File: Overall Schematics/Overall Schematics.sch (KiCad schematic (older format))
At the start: 31 parts, among them J1 WattMeter1_Output, J2 WattMeter2_Output, J3 Intel_Buck_Converter_Input, J4 WattMeter1_Input, J5 WattMeter2_Input, M1 Stepper_Motor_bipolar, M2 Stepper_Motor_bipolar, M3 LinActuator12V, M4 LinActuator12V, M5 LinActuator12V, M6 Motor_DC, M7 Motor_DC, M8 Motor_DC, M9 Motor_DC, SW1 SW_DPST, U1 Teensy4.1, U10 VNH52019, U2 36v4SMD, U3 36v4SMD, U4 VNH52019, U5 VNH52019, U6 VNH52019, U7 VNH52019, U8 VNH52019, U9 VNH52019

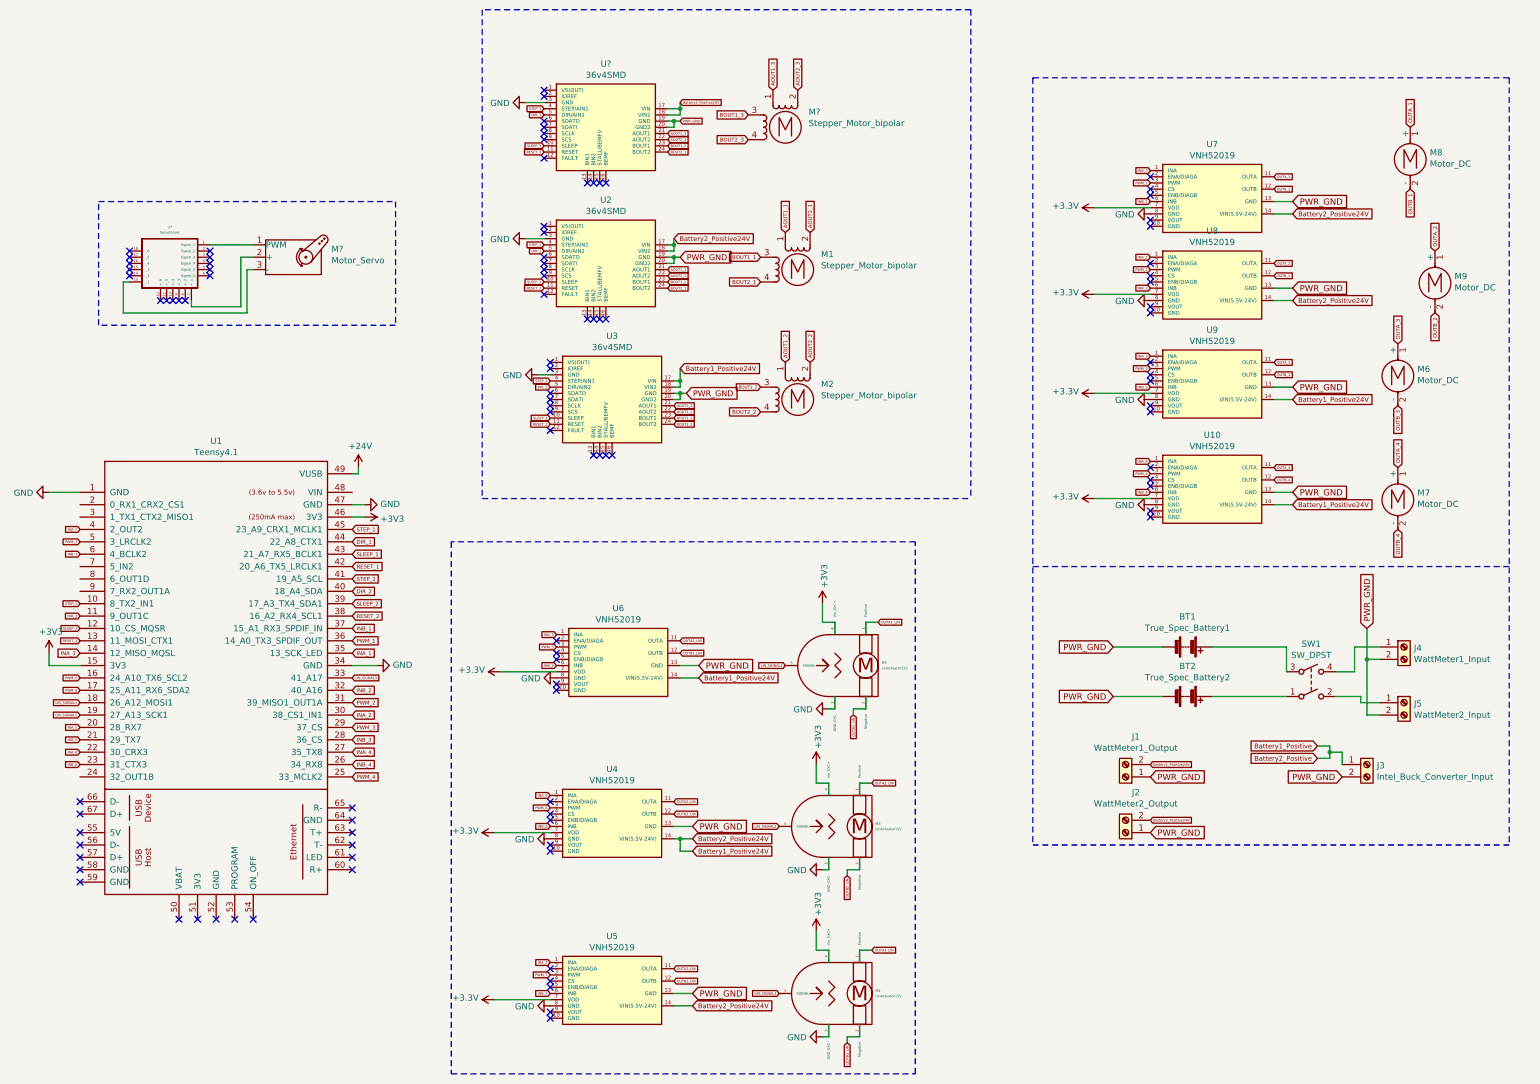
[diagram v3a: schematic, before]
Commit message: placement of ICs and proper pin connectors are pretty much done
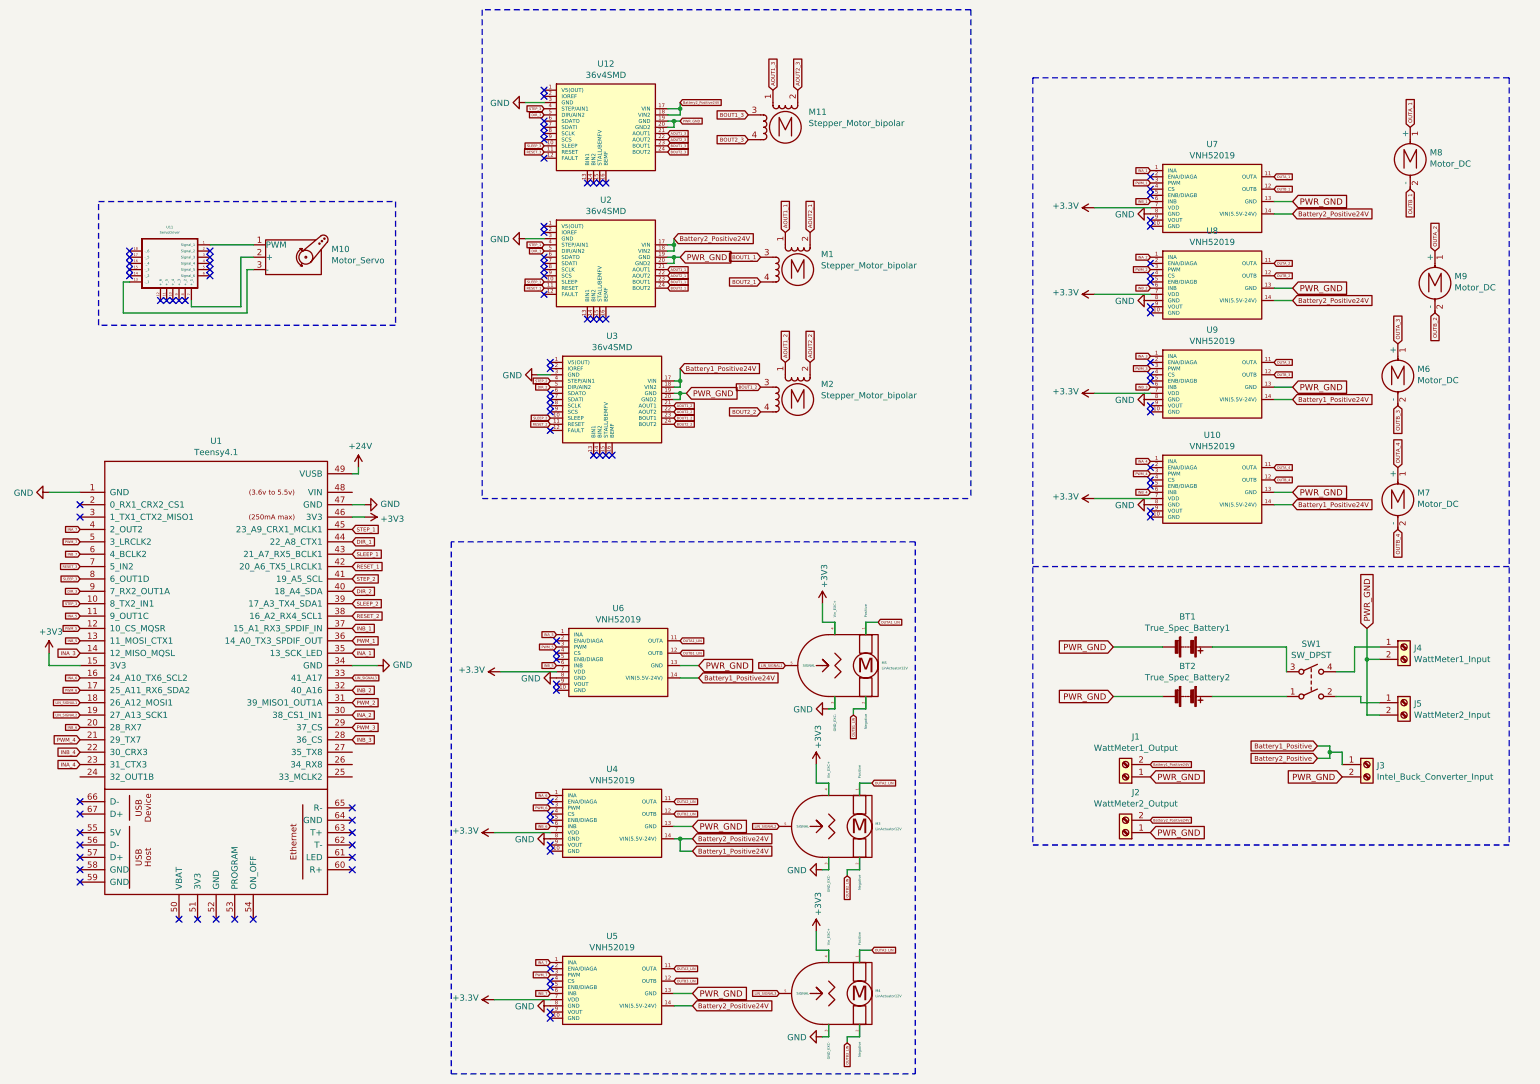
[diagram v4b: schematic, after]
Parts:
- U12: renamed from U?; footprint (none) -> Custom Footprints:StepperMotorDriver
- gave numbers to parts that had none: 3
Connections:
- net DIR_3: now also U1.9 (7_RX2_OUT1A); no longer U1.11 (9_OUT1C)
- net INA_4: now also U1.23 (31_CTX3); no longer U1.27 (35_TX8)
- net INA_5: now also U1.11 (9_OUT1C); no longer U1.20 (28_RX7)
- net INA_6: now also U1.16 (24_A10_TX6_SCL2); no longer U1.22 (30_CRX3)
- net INB_4: now also U1.22 (30_CRX3); no longer U1.26 (34_RX8)
- net INB_5: now also U1.13 (11_MOSI_CTX1); no longer U1.21 (29_TX7)
- net INB_6: now also U1.20 (28_RX7); no longer U1.23 (31_CTX3)
- net PWM_4: now also U1.21 (29_TX7); no longer U1.25 (33_MCLK2)
- net PWM_5: now also U1.12 (10_CS_MQSR); no longer U1.16 (24_A10_TX6_SCL2)
- net RESET_3: now also U1.7 (5_IN2); no longer U1.13 (11_MOSI_CTX1)
- net SLEEP_3: now also U1.8 (6_OUT1D); no longer U1.12 (10_CS_MQSR)
- no-connect marks 101 -> 103
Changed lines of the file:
@@
 Text GLabel 20950 14600 2    31   Input ~ 0
 INB_3
-Text GLabel 20950 14700 2    31   Input ~ 0
+Text GLabel 18750 14800 0    31   Input ~ 0
 INA_4
-Text GLabel 20950 14900 2    31   Input ~ 0
+Text GLabel 18750 14600 0    31   Input ~ 0
 PWM_4
-Text GLabel 20950 14800 2    31   Input ~ 0
+Text GLabel 18750 14700 0    31   Input ~ 0
 INB_4
 Text GLabel 22550 11700 0    20   Input ~ 0
@@
 Text GLabel 18750 14300 0    20   Input ~ 0
 LIN_SIGNAL1
-Text GLabel 18750 14500 0    20   Input ~ 0
+Text GLabel 18750 13600 0    20   Input ~ 0
 INA_5
-Text GLabel 18750 14100 0    20   Input ~ 0
+Text GLabel 18750 13700 0    20   Input ~ 0
 PWM_5
-Text GLabel 18750 14600 0    20   Input ~ 0
+Text GLabel 18750 13800 0    20   Input ~ 0
 INB_5
 Text GLabel 20950 13100 2    31   Input ~ 0
@@
 Text GLabel 24400 15300 0    20   Input ~ 0
 LIN_SIGNAL2
-Text GLabel 18750 14700 0    20   Input ~ 0
+Text GLabel 18750 14100 0    20   Input ~ 0
 INA_6
 Text GLabel 18750 14200 0    20   Input ~ 0
 PWM_6
-Text GLabel 18750 14800 0    20   Input ~ 0
+Text GLabel 18750 14500 0    20   Input ~ 0
 INB_6
 Text GLabel 18750 14400 0    20   Input ~ 0
@@
 	21750 17300 25500 17300
 $Comp
-L CustomLibrary:36v4SMD U?
+L CustomLibrary:36v4SMD U12
 U 1 1 6009DFB5
 P 23000 9200
-F 0 "U?" H 23000 9263 50  0000 C CNN
+F 0 "U12" H 23000 9263 50  0000 C CNN
 F 1 "36v4SMD" H 23000 9172 50  0000 C CNN
-F 2 "" H 23000 9200 50  0001 C CNN
+F 2 "Custom Footprints:StepperMotorDriver" H 23000 9200 50  0001 C CNN
 F 3 "" H 23000 9200 50  0001 C CNN
 	1    23000 9200
@@
 NoConn ~ 23000 10100
 $Comp
-L power:GND #PWR?
+L power:GND #PWR0129
 U 1 1 600BE28C
 P 22350 9450
-F 0 "#PWR?" H 22350 9200 50  0001 C CNN
+F 0 "#PWR0129" H 22350 9200 50  0001 C CNN
 F 1 "GND" V 22355 9322 50  0000 R CNN
 F 2 "" H 22350 9450 50  0001 C CNN
@@
 RESET_3
 $Comp
-L Motor:Stepper_Motor_bipolar M?
+L Motor:Stepper_Motor_bipolar M11
 U 1 1 600C6332
 P 24450 9650
-F 0 "M?" H 24638 9774 50  0000 L CNN
+F 0 "M11" H 24638 9774 50  0000 L CNN
 F 1 "Stepper_Motor_bipolar" H 24638 9683 50  0000 L CNN
 F 2 "TerminalBlock:TerminalBlock_bornier-4_P5.08mm" H 24460 9640 50  0001 C CNN
@@
 Wire Notes Line
 	30300 9250 30300 15450
-Text GLabel 18750 13800 0    20   Input ~ 0
+Text GLabel 18750 13200 0    20   Input ~ 0
 RESET_3
-Text GLabel 18750 13700 0    20   Input ~ 0
+Text GLabel 18750 13300 0    20   Input ~ 0
 SLEEP_3
-Text GLabel 18750 13600 0    20   Input ~ 0
+Text GLabel 18750 13400 0    20   Input ~ 0
 DIR_3
 Text GLabel 18750 13500 0    20   Input ~ 0
 STEP_3
 $Comp
-L CustomLibrary:ServoDriver U?
+L CustomLibrary:ServoDriver U11
 U 1 1 6010875A
 P 19450 10500
-F 0 "U?" H 19475 10543 20  0000 C CNN
+F 0 "U11" H 19475 10543 20  0000 C CNN
 F 1 "ServoDriver" H 19475 10500 20  0000 C CNN
 F 2 "" H 19450 10600 20  0001 C CNN
@@
 $EndComp
 $Comp
-L Motor:Motor_Servo M?
+L Motor:Motor_Servo M10
 U 1 1 601479AE
 P 20450 10700
-F 0 "M?" H 20782 10765 50  0000 L CNN
+F 0 "M10" H 20782 10765 50  0000 L CNN
 F 1 "Motor_Servo" H 20782 10674 50  0000 L CNN
 F 2 "" H 20450 10510 50  0001 C CNN
@@
 Wire Notes Line
 	18900 11250 18900 10250
+NoConn ~ 18750 12700
+NoConn ~ 18750 12800
 $EndSCHEMATC

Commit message: finished routing main ICs, have to figure out power routing, vary track width
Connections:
- net INA_3: now also U1.27 (35_TX8); no longer U1.14 (12_MISO_MQSL)
- net INA_6: now also U1.14 (12_MISO_MQSL); no longer U1.16 (24_A10_TX6_SCL2)
- net LIN_SIGNAL1: now also U1.17 (25_A11_RX6_SDA2); no longer U1.18 (26_A12_MOSI1)
- net LIN_SIGNAL2: now also U1.18 (26_A12_MOSI1); no longer U1.19 (27_A13_SCK1)
- net LIN_SIGNAL3: now also U1.19 (27_A13_SCK1); no longer U1.33 (41_A17)
- net PWM_6: now also U1.16 (24_A10_TX6_SCL2); no longer U1.17 (25_A11_RX6_SDA2)
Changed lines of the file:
@@
 Text GLabel 20950 14200 2    31   Input ~ 0
 INB_2
-Text GLabel 18750 13900 0    31   Input ~ 0
+Text GLabel 20950 14700 2    31   Input ~ 0
 INA_3
 Text GLabel 20950 14600 2    31   Input ~ 0
@@
 Text GLabel 24450 14000 0    20   Input ~ 0
 LIN_SIGNAL1
-Text GLabel 18750 14300 0    20   Input ~ 0
+Text GLabel 18750 14200 0    20   Input ~ 0
 LIN_SIGNAL1
 Text GLabel 18750 13600 0    20   Input ~ 0
@@
 Text GLabel 24400 15300 0    20   Input ~ 0
 LIN_SIGNAL2
+Text GLabel 18750 13900 0    20   Input ~ 0
+INA_6
 Text GLabel 18750 14100 0    20   Input ~ 0
-INA_6
-Text GLabel 18750 14200 0    20   Input ~ 0
 PWM_6
 Text GLabel 18750 14500 0    20   Input ~ 0
 INB_6
-Text GLabel 18750 14400 0    20   Input ~ 0
+Text GLabel 18750 14300 0    20   Input ~ 0
 LIN_SIGNAL2
 Wire Wire Line
@@
 Text GLabel 18750 13100 0    20   Input ~ 0
 INB_7
-Text GLabel 20950 14100 2    20   Input ~ 0
+Text GLabel 18750 14400 0    20   Input ~ 0
 LIN_SIGNAL3
 $Comp

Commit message: PCB Updates
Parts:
- M10: footprint (none) -> TerminalBlock:TerminalBlock_bornier-3_P5.08mm
- U11: footprint (none) -> Custom Footprints:ServoMotorDriver
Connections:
- net LIN_SIGNAL1: now also U1.18 (26_A12_MOSI1); no longer U1.17 (25_A11_RX6_SDA2)
- net LIN_SIGNAL2: now also U1.19 (27_A13_SCK1); no longer U1.18 (26_A12_MOSI1)
- net LIN_SIGNAL3: now also U1.17 (25_A11_RX6_SDA2); no longer U1.19 (27_A13_SCK1)
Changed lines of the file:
@@
 Text GLabel 24450 14000 0    20   Input ~ 0
 LIN_SIGNAL1
-Text GLabel 18750 14200 0    20   Input ~ 0
+Text GLabel 18750 14300 0    20   Input ~ 0
 LIN_SIGNAL1
 Text GLabel 18750 13600 0    20   Input ~ 0
@@
 Text GLabel 18750 14500 0    20   Input ~ 0
 INB_6
-Text GLabel 18750 14300 0    20   Input ~ 0
+Text GLabel 18750 14400 0    20   Input ~ 0
 LIN_SIGNAL2
 Wire Wire Line
@@
 Text GLabel 18750 13100 0    20   Input ~ 0
 INB_7
-Text GLabel 18750 14400 0    20   Input ~ 0
+Text GLabel 18750 14200 0    20   Input ~ 0
 LIN_SIGNAL3
 $Comp
@@
 F 0 "U11" H 19475 10543 20  0000 C CNN
 F 1 "ServoDriver" H 19475 10500 20  0000 C CNN
-F 2 "" H 19450 10600 20  0001 C CNN
+F 2 "Custom Footprints:ServoMotorDriver" H 19450 10600 20  0001 C CNN
 F 3 "" H 19450 10600 20  0001 C CNN
 	1    19450 10500
@@
 F 0 "M10" H 20782 10765 50  0000 L CNN
 F 1 "Motor_Servo" H 20782 10674 50  0000 L CNN
-F 2 "" H 20450 10510 50  0001 C CNN
+F 2 "TerminalBlock:TerminalBlock_bornier-3_P5.08mm" H 20450 10510 50  0001 C CNN
 F 3 "http://forums.parallax.com/uploads/attachments/46831/74481.png" H 20450 10510 50  0001 C CNN
 	1    20450 10700
